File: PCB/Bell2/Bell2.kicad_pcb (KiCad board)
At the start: 2 copper layers, 38.3 x 28.7 mm, 38 parts, among them J1 USB-C, J2 POWER, J3 Conn_01x08, J4 Shelly, J5 Conn_01x05, J6 Conn_01x02, U1 ESP32-PICO-MINI-02, U2 FT231XQ, U3 ISL89410, U4 ISL89410, U5 LMR16006XDDCR, U7 AA, U8 QR

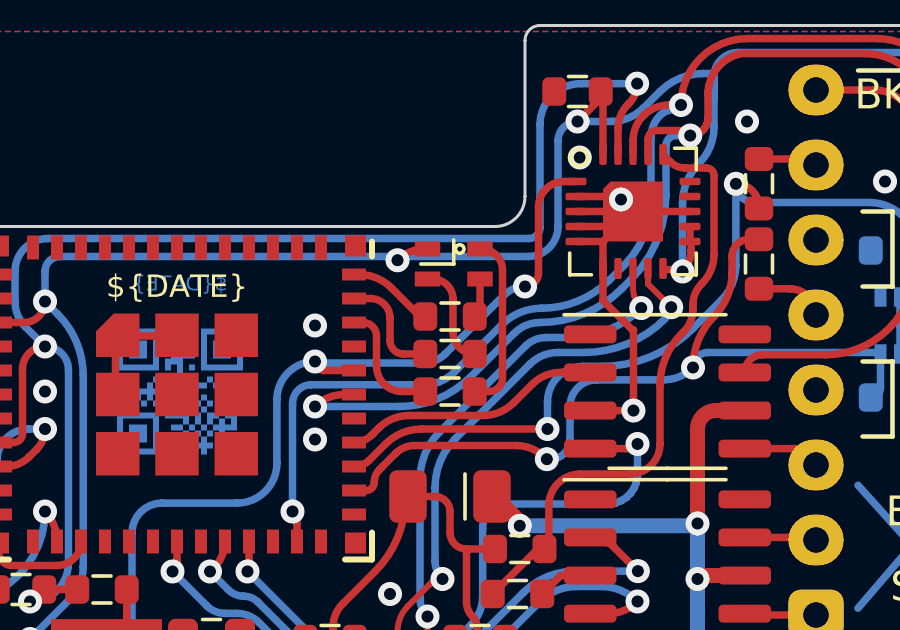
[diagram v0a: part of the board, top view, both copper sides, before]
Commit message: New LED
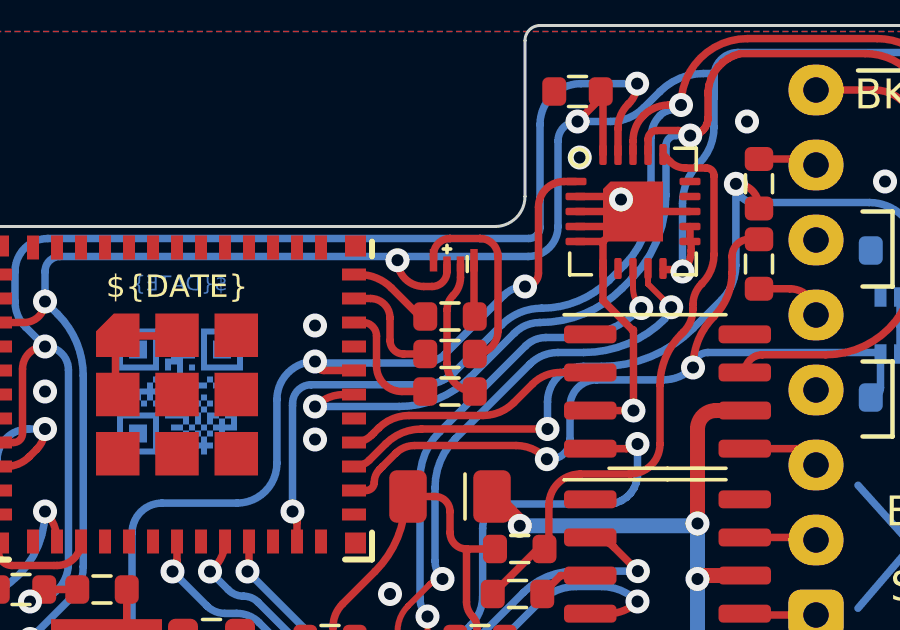
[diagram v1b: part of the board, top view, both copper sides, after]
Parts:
- D2: value LED_RGBA -> LED_BARG; footprint RevK:LED-RGB-1.6x1.6 -> RevK:MHS190RGBCT
- R10: value 220R -> 100R
- R8: value 680R -> 300R
- R9: value 2K -> 1K
- turned D2 to 0 degrees
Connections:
- D2 pad 1: +3V3 -> Net-(D2-Pad1)
- D2 pad 2: Net-(D2-Pad2) -> +3V3
- R10 pad 1: Net-(D2-Pad4) -> Net-(D2-Pad1)
- R8 pad 1: Net-(D2-Pad2) -> Net-(D2-Pad3)
- R9 pad 1: Net-(D2-Pad3) -> Net-(D2-Pad4)
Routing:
- net Net-(D2-Pad1): track 0.00 -> 6.60 mm
- net Net-(D2-Pad2): track 5.83 -> 0.00 mm
- net Net-(D2-Pad3): track 1.08 -> 4.85 mm
- net +3V3: track 97.6 -> 99.3 mm
- net Net-(D2-Pad4): track 3.24 -> 1.88 mm

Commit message: 3D update
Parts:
- J5: moved to B.Cu
- turned J5 to 90 degrees
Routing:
- net GPSTICK: track 16.9 -> 11.5 mm
- net GPSRX: track 5.66 -> 10.9 mm
- net +3V3: track 99.3 -> 103.0 mm
- net GPSTX: track 9.71 -> 9.89 mm, vias 0 -> 1
